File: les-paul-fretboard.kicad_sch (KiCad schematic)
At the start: 13 parts, among them J1 Conn_01x10_Female, J2 Conn_01x10_Female, SW1 Green(A), SW2 Red(B), SW3 Yellow(Y), SW4 Blue(X), SW5 Orange(TB), U1 SN74LV1T34DBV

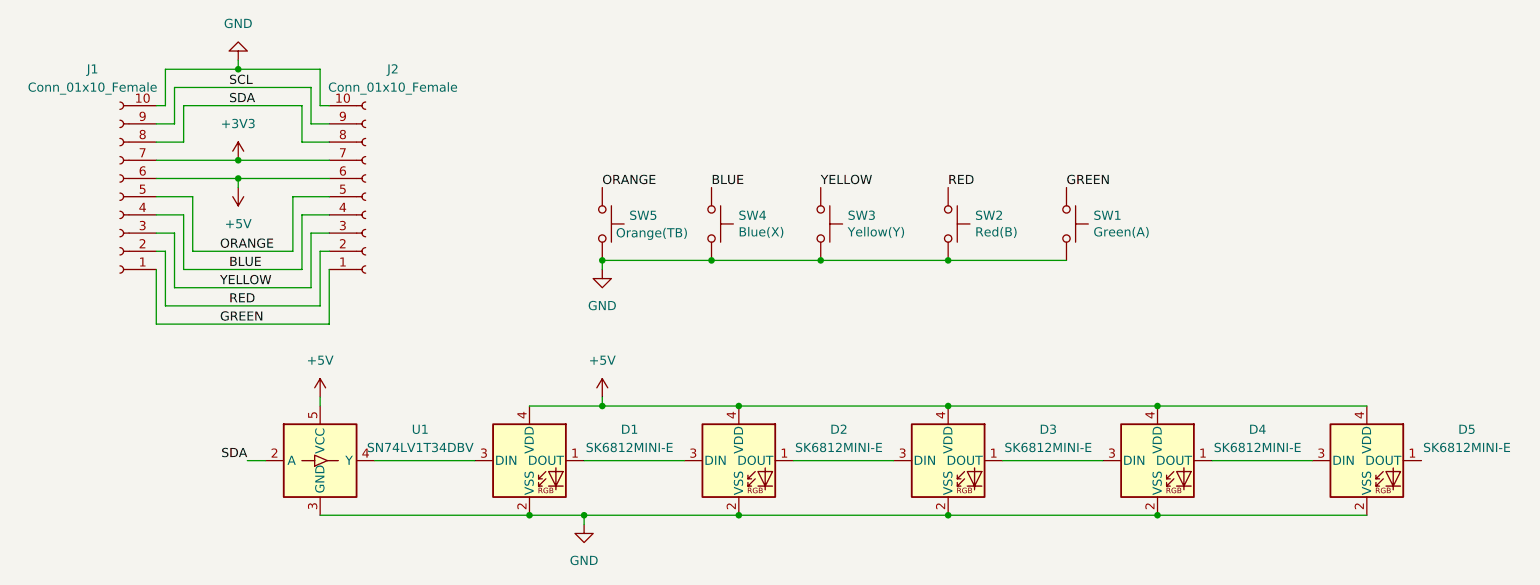
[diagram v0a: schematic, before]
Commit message: Replace LED footprint with intended footprint (pin layout was wrong)
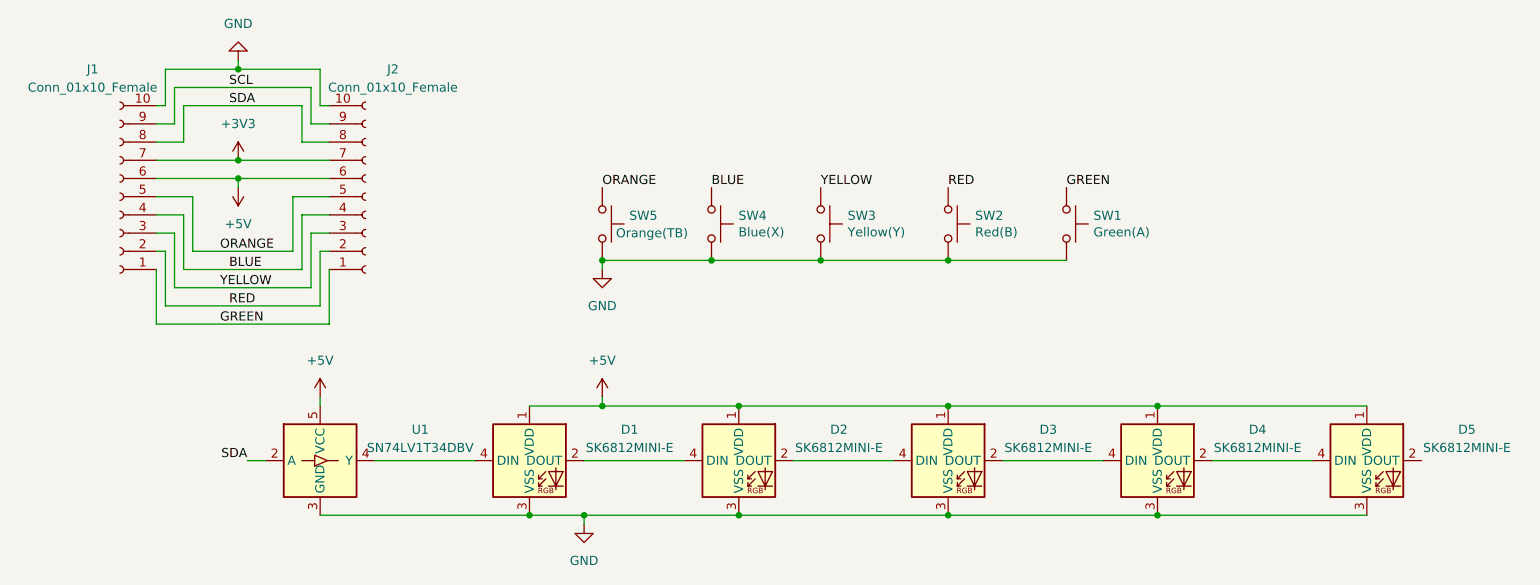
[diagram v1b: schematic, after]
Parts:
- D1, D2, D3, D4, D5: footprint Keebio-Parts:SK6812-MINI-E -> SK6812MINI-E:SK6812MINI-E-Vias; symbol LED:SK6812MINI -> SK6812MINI-E:SK6812MINI-E
- J2: footprint (none) -> Connector_PinHeader_2.00mm:PinHeader_1x10_P2.00mm_Horizontal
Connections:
- net +5V: now also D1.1 (VDD), D2.1 (VDD), D3.1 (VDD), D4.1 (VDD), D5.1 (VDD); no longer D1.4 (VDD), D2.4 (VDD), D3.4 (VDD), D4.4 (VDD), D5.4 (VDD)
- net GND: now also D1.3 (VSS), D2.3 (VSS), D3.3 (VSS), D4.3 (VSS), D5.3 (VSS); no longer D1.2 (VSS), D2.2 (VSS), D3.2 (VSS), D4.2 (VSS), D5.2 (VSS)
- net at U1.4 (Y): now also D1.4 (DIN); no longer D1.3 (DIN)
- new net: D1.2 (DOUT), D2.4 (DIN)
- new net: D4.2 (DOUT), D5.4 (DIN)
- new net: D3.2 (DOUT), D4.4 (DIN)
- new net: D2.2 (DOUT), D3.4 (DIN)
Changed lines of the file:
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@@
     (pin "1")
   )
-  (symbol (lib_id "LED:SK6812MINI") (at 85.09 121.92 0) (unit 1)
+  (symbol (lib_id "SK6812MINI-E:SK6812MINI-E") (at 85.09 121.92 0) (unit 1)
     (in_bom yes) (on_board yes) (fields_autoplaced)
     (property "Reference" "D1" (id 0) (at 99.06 117.5893 0))
     (property "Value" "SK6812MINI-E" (id 1) (at 99.06 120.1293 0))
-    (property "Footprint" "Keebio-Parts:SK6812-MINI-E" (id 2) (at 86.36 129.54 0)
-      (effects (font (size 1.27 1.27)) (justify left top) hide)
-    )
-    (property "Datasheet" "https://cdn-shop.adafruit.com/product-files/2686/SK6812MINI_REV.01-1-2.pdf" (id 3) (at 87.63 131.445 0)
-      (effects (font (size 1.27 1.27)) (justify left top) hide)
+    (property "Footprint" "SK6812MINI-E:SK6812MINI-E-Vias" (id 2) (at 101.6 130.81 0)
+      (effects (font (size 1.27 1.27)) hide)
+    )
+    (property "Datasheet" "https://cdn-shop.adafruit.com/product-files/2686/SK6812MINI_REV.01-1-2.pdf" (id 3) (at 85.09 121.92 0)
+      (effects (font (size 1.27 1.27)) hide)
     )
     (pin "1")
@@
     (pin "9")
   )
-  (symbol (lib_id "LED:SK6812MINI") (at 172.72 121.92 0) (unit 1)
+  (symbol (lib_id "SK6812MINI-E:SK6812MINI-E") (at 172.72 121.92 0) (unit 1)
     (in_bom yes) (on_board yes) (fields_autoplaced)
     (property "Reference" "D4" (id 0) (at 186.69 117.5893 0))
     (property "Value" "SK6812MINI-E" (id 1) (at 186.69 120.1293 0))
-    (property "Footprint" "Keebio-Parts:SK6812-MINI-E" (id 2) (at 173.99 129.54 0)
-      (effects (font (size 1.27 1.27)) (justify left top) hide)
-    )
-    (property "Datasheet" "https://cdn-shop.adafruit.com/product-files/2686/SK6812MINI_REV.01-1-2.pdf" (id 3) (at 175.26 131.445 0)
-      (effects (font (size 1.27 1.27)) (justify left top) hide)
-    )
-    (pin "1")
-    (pin "2")
-    (pin "3")
-    (pin "4")
-  )
-  (symbol (lib_id "LED:SK6812MINI") (at 143.51 121.92 0) (unit 1)
+    (property "Footprint" "SK6812MINI-E:SK6812MINI-E-Vias" (id 2) (at 189.23 130.81 0)
+      (effects (font (size 1.27 1.27)) hide)
+    )
+    (property "Datasheet" "https://cdn-shop.adafruit.com/product-files/2686/SK6812MINI_REV.01-1-2.pdf" (id 3) (at 172.72 121.92 0)
+      (effects (font (size 1.27 1.27)) hide)
+    )
+    (pin "1")
+    (pin "2")
+    (pin "3")
+    (pin "4")
+  )
+  (symbol (lib_id "SK6812MINI-E:SK6812MINI-E") (at 143.51 121.92 0) (unit 1)
     (in_bom yes) (on_board yes) (fields_autoplaced)
     (property "Reference" "D3" (id 0) (at 157.48 117.5893 0))
     (property "Value" "SK6812MINI-E" (id 1) (at 157.48 120.1293 0))
-    (property "Footprint" "Keebio-Parts:SK6812-MINI-E" (id 2) (at 144.78 129.54 0)
-      (effects (font (size 1.27 1.27)) (justify left top) hide)
-    )
-    (property "Datasheet" "https://cdn-shop.adafruit.com/product-files/2686/SK6812MINI_REV.01-1-2.pdf" (id 3) (at 146.05 131.445 0)
-      (effects (font (size 1.27 1.27)) (justify left top) hide)
+    (property "Footprint" "SK6812MINI-E:SK6812MINI-E-Vias" (id 2) (at 160.02 130.81 0)
+      (effects (font (size 1.27 1.27)) hide)
+    )
+    (property "Datasheet" "https://cdn-shop.adafruit.com/product-files/2686/SK6812MINI_REV.01-1-2.pdf" (id 3) (at 143.51 121.92 0)
+      (effects (font (size 1.27 1.27)) hide)
     )
     (pin "1")
@@
     (property "Reference" "J2" (id 0) (at 66.04 67.31 0))
     (property "Value" "Conn_01x10_Female" (id 1) (at 66.04 69.85 0))
-    (property "Footprint" "" (id 2) (at 62.23 85.09 0)
+    (property "Footprint" "Connector_PinHeader_2.00mm:PinHeader_1x10_P2.00mm_Horizontal" (id 2) (at 62.23 85.09 0)
       (effects (font (size 1.27 1.27)) hide)
     )
@@
     (pin "9")
   )
-  (symbol (lib_id "LED:SK6812MINI") (at 201.93 121.92 0) (unit 1)
+  (symbol (lib_id "SK6812MINI-E:SK6812MINI-E") (at 201.93 121.92 0) (unit 1)
     (in_bom yes) (on_board yes) (fields_autoplaced)
     (property "Reference" "D5" (id 0) (at 215.9 117.5893 0))
     (property "Value" "SK6812MINI-E" (id 1) (at 215.9 120.1293 0))
-    (property "Footprint" "Keebio-Parts:SK6812-MINI-E" (id 2) (at 203.2 129.54 0)
-      (effects (font (size 1.27 1.27)) (justify left top) hide)
-    )
-    (property "Datasheet" "https://cdn-shop.adafruit.com/product-files/2686/SK6812MINI_REV.01-1-2.pdf" (id 3) (at 204.47 131.445 0)
-      (effects (font (size 1.27 1.27)) (justify left top) hide)
+    (property "Footprint" "SK6812MINI-E:SK6812MINI-E-Vias" (id 2) (at 218.44 130.81 0)
+      (effects (font (size 1.27 1.27)) hide)
+    )
+    (property "Datasheet" "https://cdn-shop.adafruit.com/product-files/2686/SK6812MINI_REV.01-1-2.pdf" (id 3) (at 201.93 121.92 0)
+      (effects (font (size 1.27 1.27)) hide)
     )
     (pin "1")
@@
     (pin "1")
   )
-  (symbol (lib_id "LED:SK6812MINI") (at 114.3 121.92 0) (unit 1)
+  (symbol (lib_id "SK6812MINI-E:SK6812MINI-E") (at 114.3 121.92 0) (unit 1)
     (in_bom yes) (on_board yes) (fields_autoplaced)
     (property "Reference" "D2" (id 0) (at 128.27 117.5893 0))
     (property "Value" "SK6812MINI-E" (id 1) (at 128.27 120.1293 0))
-    (property "Footprint" "Keebio-Parts:SK6812-MINI-E" (id 2) (at 115.57 129.54 0)
-      (effects (font (size 1.27 1.27)) (justify left top) hide)
-    )
-    (property "Datasheet" "https://cdn-shop.adafruit.com/product-files/2686/SK6812MINI_REV.01-1-2.pdf" (id 3) (at 116.84 131.445 0)
-      (effects (font (size 1.27 1.27)) (justify left top) hide)
+    (property "Footprint" "SK6812MINI-E:SK6812MINI-E-Vias" (id 2) (at 130.81 130.81 0)
+      (effects (font (size 1.27 1.27)) hide)
+    )
+    (property "Datasheet" "https://cdn-shop.adafruit.com/product-files/2686/SK6812MINI_REV.01-1-2.pdf" (id 3) (at 114.3 121.92 0)
+      (effects (font (size 1.27 1.27)) hide)
     )
     (pin "1")
@@
     )
     (path "/4822e50f-e785-47d2-aa10-e22d4f4fd65b"
-      (reference "D1") (unit 1) (value "SK6812MINI-E") (footprint "Keebio-Parts:SK6812-MINI-E")
+      (reference "D1") (unit 1) (value "SK6812MINI-E") (footprint "SK6812MINI-E:SK6812MINI-E-Vias")
     )
     (path "/e1f14a08-1943-42e6-95fe-46e65370dac6"
-      (reference "D2") (unit 1) (value "SK6812MINI-E") (footprint "Keebio-Parts:SK6812-MINI-E")
+      (reference "D2") (unit 1) (value "SK6812MINI-E") (footprint "SK6812MINI-E:SK6812MINI-E-Vias")
     )
     (path "/87ecb998-f065-4bba-bb15-90775bfec37f"
-      (reference "D3") (unit 1) (value "SK6812MINI-E") (footprint "Keebio-Parts:SK6812-MINI-E")
+      (reference "D3") (unit 1) (value "SK6812MINI-E") (footprint "SK6812MINI-E:SK6812MINI-E-Vias")
     )
     (path "/6211dc2d-e164-423a-ab66-e0d6b35757d4"
-      (reference "D4") (unit 1) (value "SK6812MINI-E") (footprint "Keebio-Parts:SK6812-MINI-E")
+      (reference "D4") (unit 1) (value "SK6812MINI-E") (footprint "SK6812MINI-E:SK6812MINI-E-Vias")
     )
     (path "/b231af28-4749-4557-aedd-d64172100b4e"
-      (reference "D5") (unit 1) (value "SK6812MINI-E") (footprint "Keebio-Parts:SK6812-MINI-E")
+      (reference "D5") (unit 1) (value "SK6812MINI-E") (footprint "SK6812MINI-E:SK6812MINI-E-Vias")
     )
     (path "/4d466c46-4f4b-4155-95ef-c69a4f3c11fa"
